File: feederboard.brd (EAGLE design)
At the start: 100 x 80 mm, 19 parts, among them IC1 TINY13V-10SU, J1 CON_HEADER_PRG_AVR_ICSP_ETCH

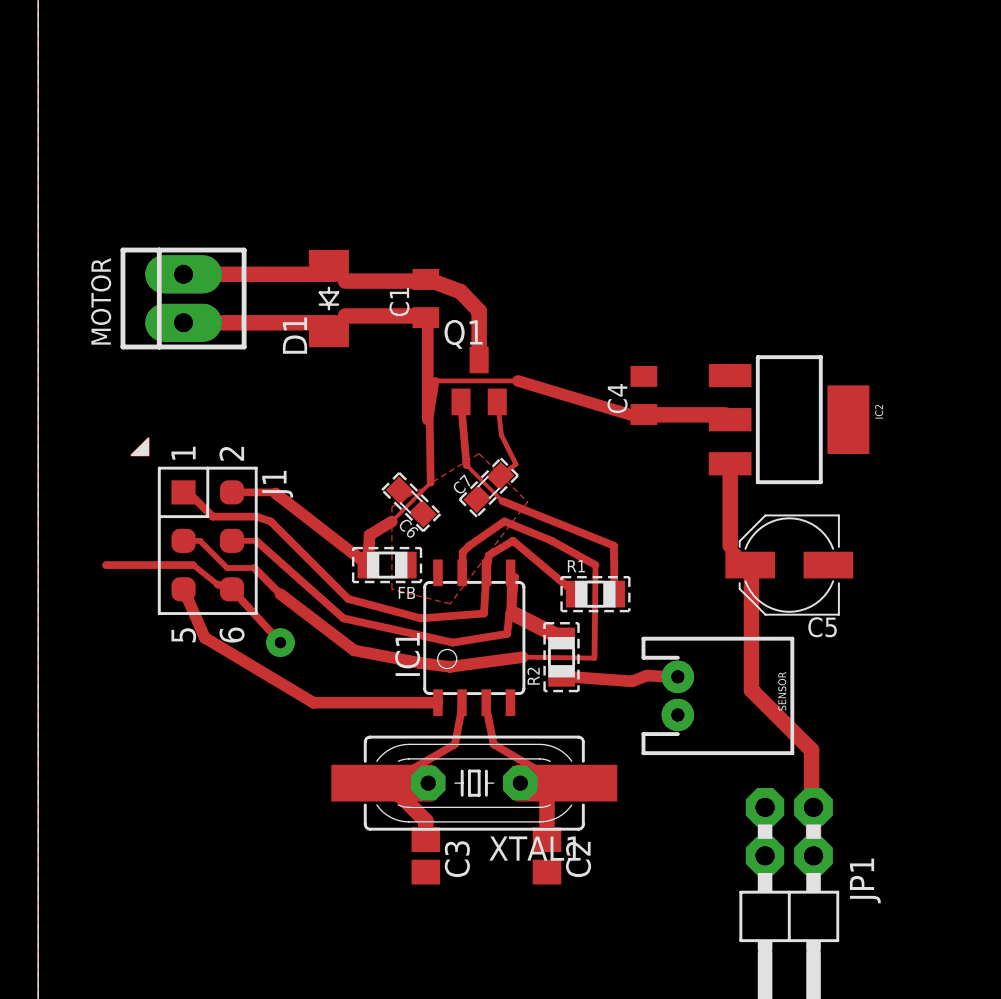
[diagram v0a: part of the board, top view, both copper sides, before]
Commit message: Pullup for reset
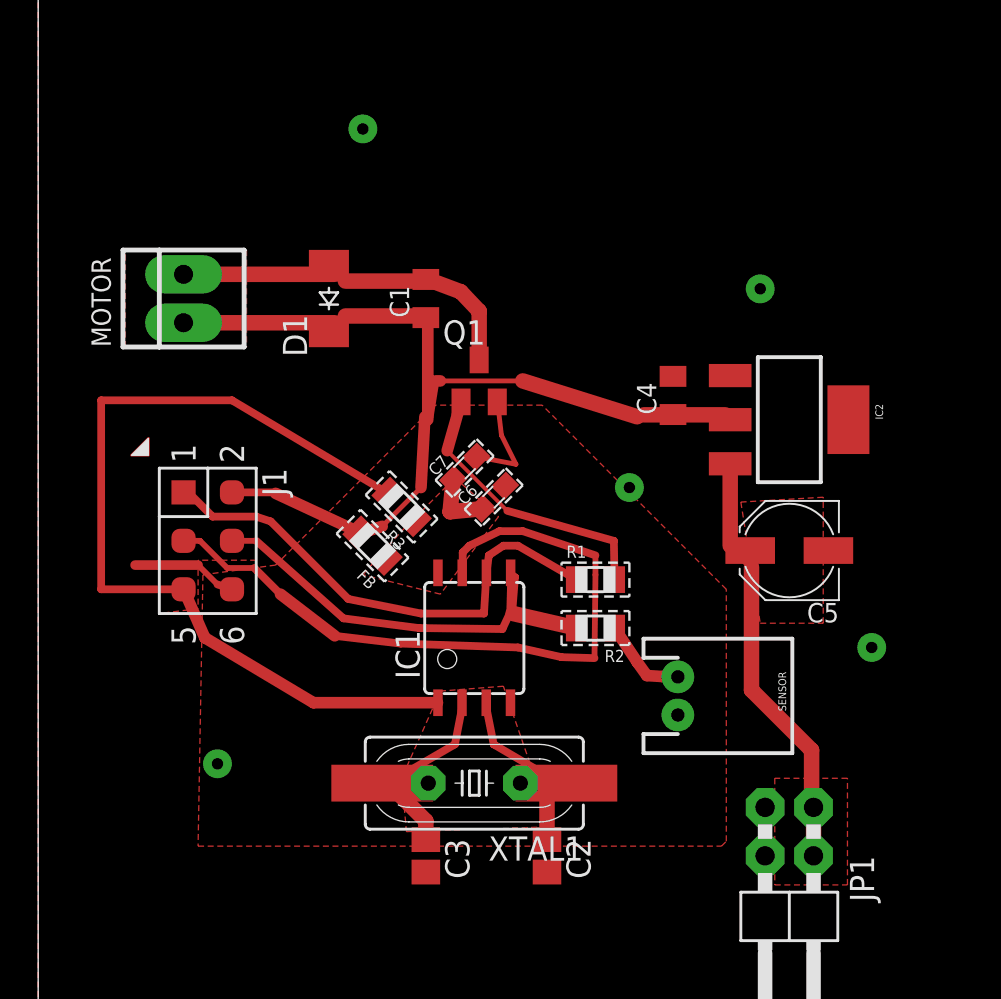
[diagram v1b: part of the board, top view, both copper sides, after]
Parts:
- added R3: 100k, LL:R0805
- moved C6 4.33 mm to (23.9, 30.2), turned to 45 degrees
- moved R2 2.34 mm to (29.2, 23.4), turned to 180 degrees
- moved C7 1.63 mm to (22.4, 31.8)
- moved C4 1.52 mm to (33.3, 35.6)
- moved FB 1.27 mm to (17.5, 27.7), turned to 135 degrees
- moved R1 0.76 mm to (29.2, 25.9)
- moved C5 0.76 mm to (39.4, 27.4)
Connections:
- net N$8 renamed VIN
- removed net VCCF: C6.1, C7.1, FB.1, IC1.8
- new net VCC: C6.1, C7.1, FB.1, IC1.8, R3.1
- net RST: now also R3.2
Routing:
- net RST: track 15.9 -> 46.5 mm
- net GND: track 15.3 -> 11.1 mm, vias 1 -> 5
- net VCC: track 0.00 -> 3.44 mm
- net SWITCH: track 6.17 -> 4.64 mm
- net VIN: track 22.4 -> 23.8 mm
- net 5V: track 55.1 -> 56.2 mm
- net MISO: track 27.0 -> 26.4 mm
- added copper zone on layer 1, net N$6
- added copper zone on layer 1, net N$7
- added copper zone on layer 1, net N$8
- added copper zone on layer 1, net N$9
- added copper zone on layer 1, net VCC
- removed copper zone on layer 1, net VCCF

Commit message: Add silk for printing
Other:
- board size 100 x 80 mm -> 69 x 55.6 mm
- board text added: "LL's CatFeeder v1.0 2013-03-24"
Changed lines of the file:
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@@
 <board>
 <plain>
-<wire x1="0" y1="0" x2="100" y2="0" width="0" layer="20"/>
-<wire x1="100" y1="0" x2="100" y2="80" width="0" layer="20"/>
-<wire x1="100" y1="80" x2="0" y2="80" width="0" layer="20"/>
-<wire x1="0" y1="80" x2="0" y2="0" width="0" layer="20"/>
+<wire x1="0" y1="0" x2="68.758" y2="0" width="0" layer="20"/>
+<wire x1="68.758" y1="0" x2="69.012" y2="55.616" width="0" layer="20"/>
+<wire x1="69.012" y1="55.616" x2="0" y2="55.616" width="0" layer="20"/>
+<wire x1="0" y1="55.616" x2="0" y2="0" width="0" layer="20"/>
+<text x="19.558" y="45.72" size="2.1844" layer="1" font="vector" ratio="16">LL's CatFeeder v1.0
+ 2013-03-24</text>
 </plain>
 <attributes>
@@
 <contactref element="JP1" pad="4"/>
 <polygon width="0.4064" layer="1" spacing="0.8128" pour="hatch" isolate="0.4064" rank="3">
-<vertex x="0" y="62.23"/>
-<vertex x="55.88" y="62.23"/>
-<vertex x="55.88" y="0"/>
+<vertex x="0" y="55.372"/>
+<vertex x="68.58" y="55.626"/>
+<vertex x="69.088" y="-1.016"/>
 <vertex x="0" y="0"/>
 </polygon>
@@
 </polygon>
 </signal>
+<signal name="N$10">
+<via x="5.08" y="50.292" extent="1-16" drill="3.2" diameter="10.16" shape="square"/>
+<via x="62.738" y="49.784" extent="1-16" drill="3.2" diameter="10.16" shape="square"/>
+<wire x1="5.08" y1="50.292" x2="62.738" y2="49.784" width="0" layer="19" extent="1-1"/>
+</signal>
 </signals>
-<errors>
-</errors>
 </board>
 </drawing>
+<compatibility>
+<note version="6.3" minversion="6.2.2" severity="warning">
+Since Version 6.2.2 text objects can contain more than one line,
+which will not be processed correctly with this version.
+</note>
+</compatibility>
 </eagle>

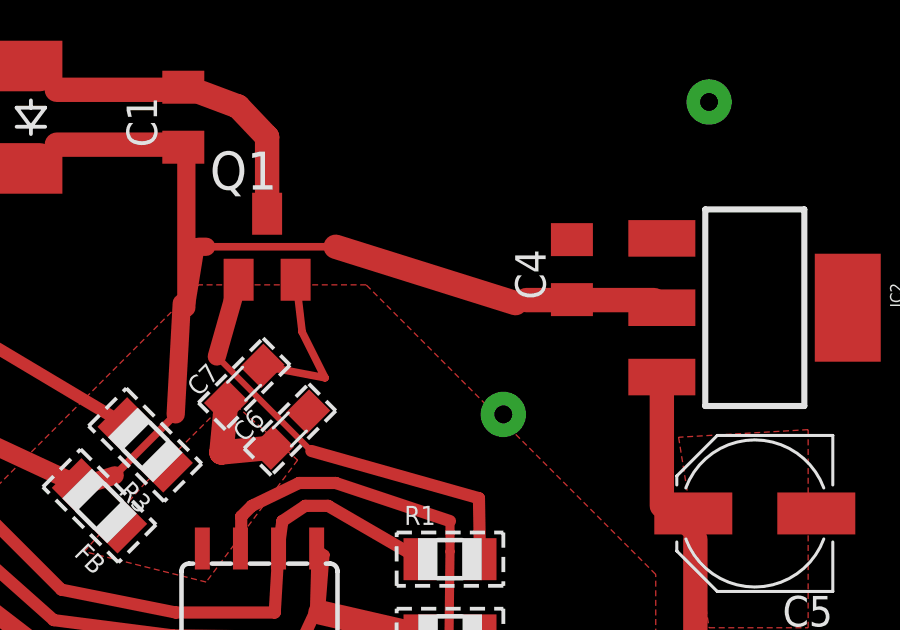
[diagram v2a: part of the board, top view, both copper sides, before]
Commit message: Add PTC fuse on 5V rail
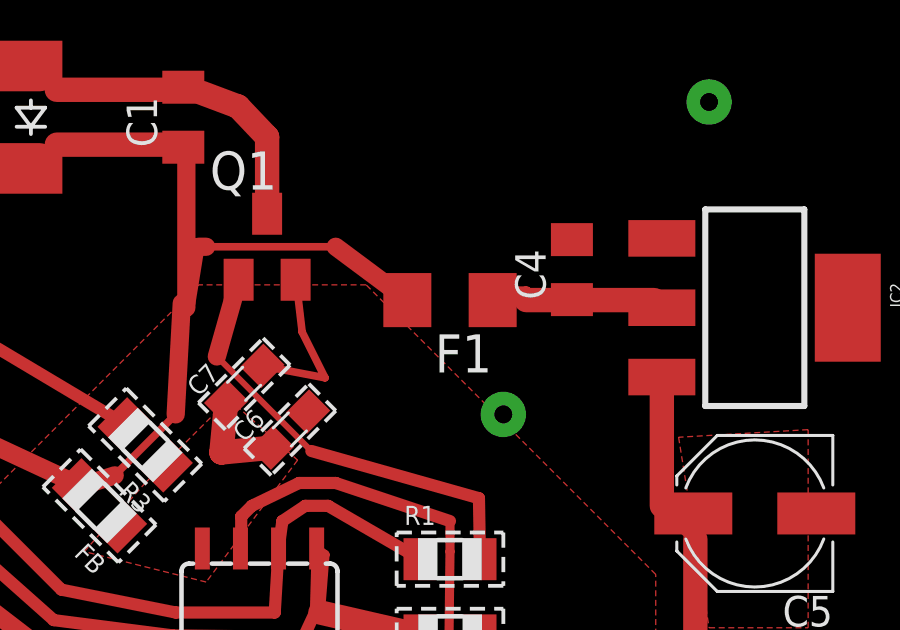
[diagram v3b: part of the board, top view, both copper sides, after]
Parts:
- added F1: (no value), adafruit:R1206
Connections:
- new net VR-OUTSM: C4.1, F1.1, IC2.2
- net 5V: now also F1.2; no longer C4.1, IC2.2
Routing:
- net 5V: track 56.2 -> 44.9 mm
- net VR-OUTSM: track 0.00 -> 7.96 mm
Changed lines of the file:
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@@
 <element name="JP1" library="pinhead" package="2X02/90" value="" x="39.37" y="7.62" rot="R180"/>
 <element name="R3" library="LL" package="R0805" value="100k" x="19.05" y="29.718" rot="R135"/>
+<element name="F1" library="adafruit" package="R1206" value="" x="29.21" y="34.544" rot="R180"/>
 </elements>
 <signals>
@@
 <contactref element="J1" pad="2"/>
 <contactref element="FB" pad="2"/>
-<contactref element="IC2" pad="2"/>
-<contactref element="C4" pad="1"/>
 <wire x1="16.1036" y1="39.7256" x2="20.32" y2="39.7256" width="0.8128" layer="1"/>
 <wire x1="15.24" y1="38.862" x2="16.1036" y2="39.7256" width="0.3048" layer="1"/>
 <wire x1="20.32" y1="39.7256" x2="20.32" y2="39.64" width="0.3048" layer="1"/>
 <wire x1="15.24" y1="38.862" x2="15.24" y2="38.84" width="0.3048" layer="1"/>
-<wire x1="36.0172" y1="34.544" x2="31.75" y2="34.544" width="0.8128" layer="1"/>
-<wire x1="36.2712" y1="34.29" x2="36.0172" y2="34.544" width="0.3048" layer="1"/>
-<wire x1="31.75" y1="34.544" x2="33.274" y2="34.56" width="0.3048" layer="1"/>
 <wire x1="12.2428" y1="30.48" x2="10.16" y2="30.48" width="0.4064" layer="1"/>
 <wire x1="12.446" y1="30.4292" x2="12.2428" y2="30.48" width="0.3048" layer="1"/>
@@
 <wire x1="20.828" y1="36.322" x2="21.082" y2="36.322" width="0.6096" layer="1"/>
 <wire x1="21.082" y1="36.322" x2="25.4" y2="36.322" width="0.254" layer="1"/>
-<wire x1="25.4" y1="36.322" x2="31.3944" y2="34.4424" width="0.8128" layer="1"/>
 <wire x1="16.6116" y1="28.2448" x2="18.034" y2="28.702" width="0.6096" layer="1"/>
 <wire x1="18.034" y1="28.702" x2="20.066" y2="30.734" width="0.254" layer="1"/>
 <wire x1="20.066" y1="30.734" x2="20.2692" y2="34.4424" width="0.6096" layer="1"/>
 <wire x1="20.2692" y1="34.4424" x2="20.5232" y2="34.4424" width="0.3048" layer="1"/>
-<wire x1="31.3944" y1="34.4424" x2="33.274" y2="34.56" width="0.3048" layer="1"/>
 <wire x1="16.6116" y1="28.2448" x2="16.818890625" y2="28.39310625" width="0.6096" layer="1"/>
 <wire x1="20.4216" y1="34.29" x2="20.4216" y2="39.624" width="0.6096" layer="1"/>
@@
 <wire x1="15.5448" y1="39.37" x2="7.62" y2="39.37" width="0.8128" layer="1"/>
 <wire x1="15.5448" y1="39.37" x2="15.24" y2="38.84" width="0.3048" layer="1"/>
+<contactref element="F1" pad="2"/>
+<wire x1="27.788" y1="34.544" x2="25.4" y2="36.322" width="0.6096" layer="1"/>
 </signal>
 <signal name="GND" airwireshidden="yes">
@@
 <wire x1="5.08" y1="50.292" x2="62.738" y2="49.784" width="0" layer="19" extent="1-1"/>
 </signal>
+<signal name="VR-OUTSM">
+<contactref element="IC2" pad="2"/>
+<contactref element="C4" pad="1"/>
+<contactref element="F1" pad="1"/>
+<wire x1="36.0172" y1="34.544" x2="31.75" y2="34.544" width="0.8128" layer="1"/>
+<wire x1="36.2712" y1="34.29" x2="36.0172" y2="34.544" width="0.3048" layer="1"/>
+<wire x1="31.75" y1="34.544" x2="33.274" y2="34.56" width="0.3048" layer="1"/>
+<wire x1="30.632" y1="34.544" x2="31.242" y2="35.052" width="0.4064" layer="1"/>
+<wire x1="31.242" y1="35.052" x2="31.242" y2="34.798" width="0.4064" layer="1"/>
+<wire x1="31.242" y1="34.798" x2="31.75" y2="34.798" width="0.4064" layer="1"/>
+<wire x1="31.75" y1="34.798" x2="31.75" y2="34.544" width="0.4064" layer="1"/>
+</signal>
 </signals>
